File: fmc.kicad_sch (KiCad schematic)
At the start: 2 parts, among them P1 ASP-134604-01, P2 ASP-134604-01

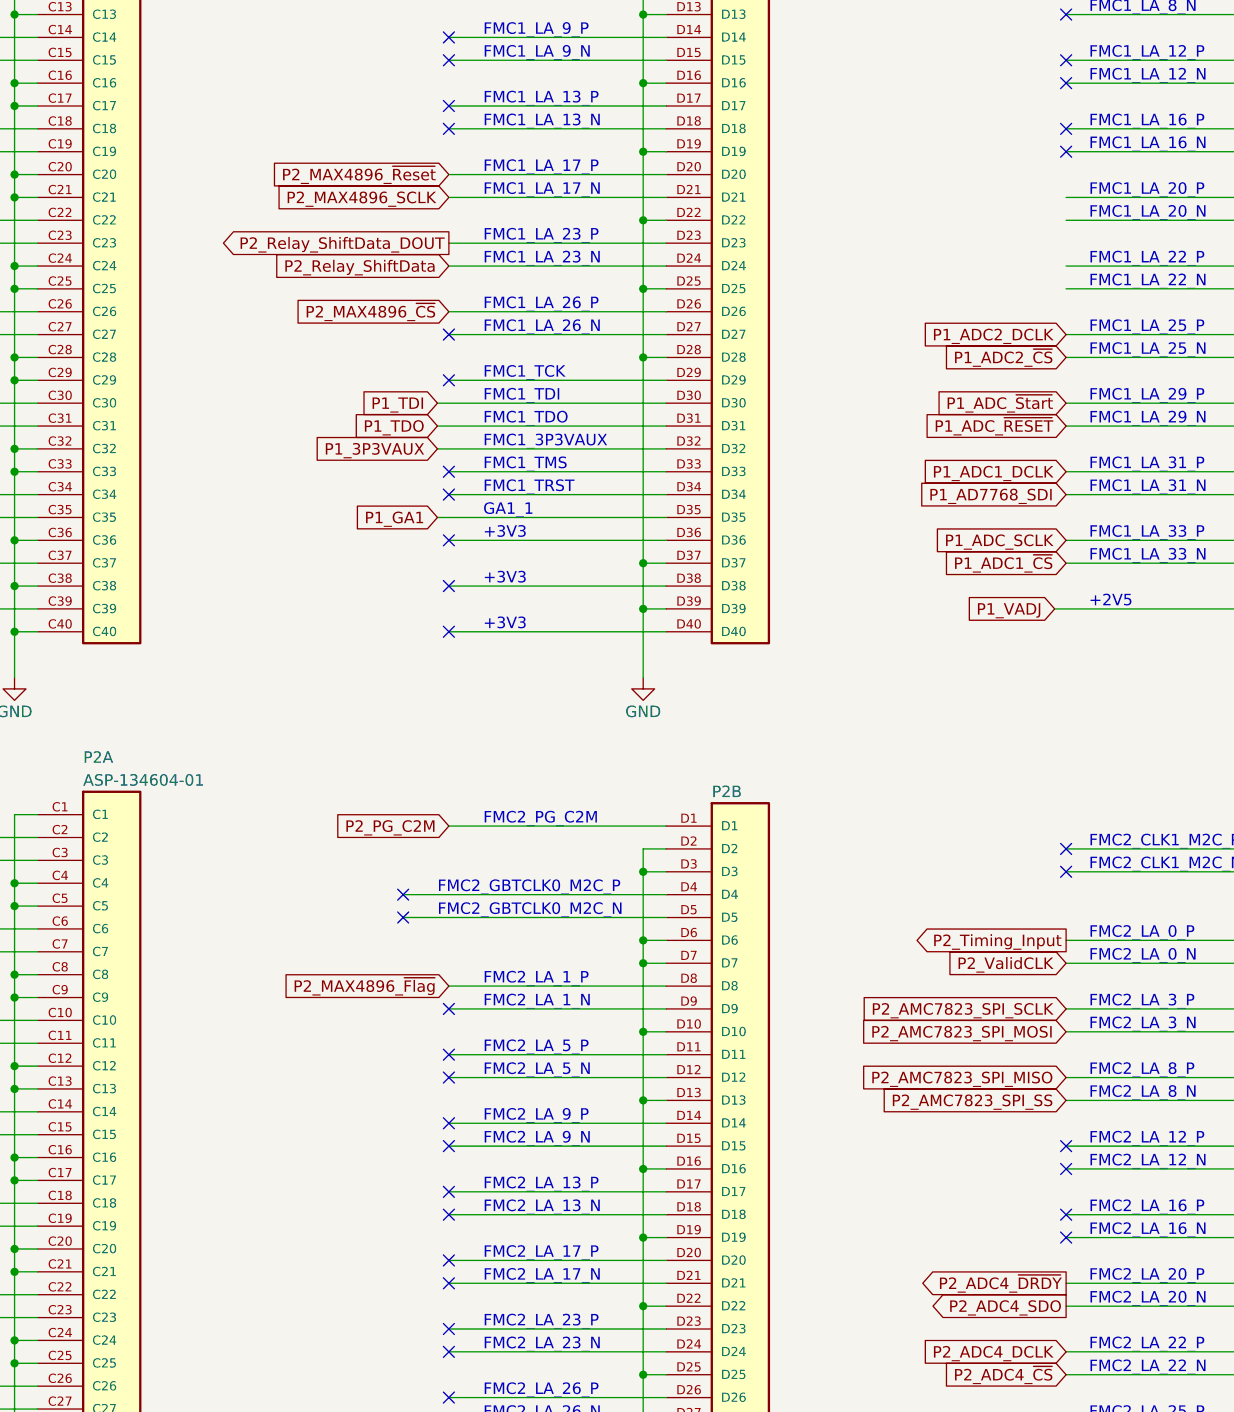
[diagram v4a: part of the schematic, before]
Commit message: Updated Project with Latest Changes
Project:
-Added pdf plots of PCB layout

Schematics:
-Fixed L8 Pinout
-Adjusted FMC connections
-Adjusted level shifter connections

Layout:
-Completed AFE/ADC/Power/Relay driver sections

Layout WIP To Complete:
-Misc. error cleanup
- Silkscreen adjust
- Add Silkscreen SN & logo
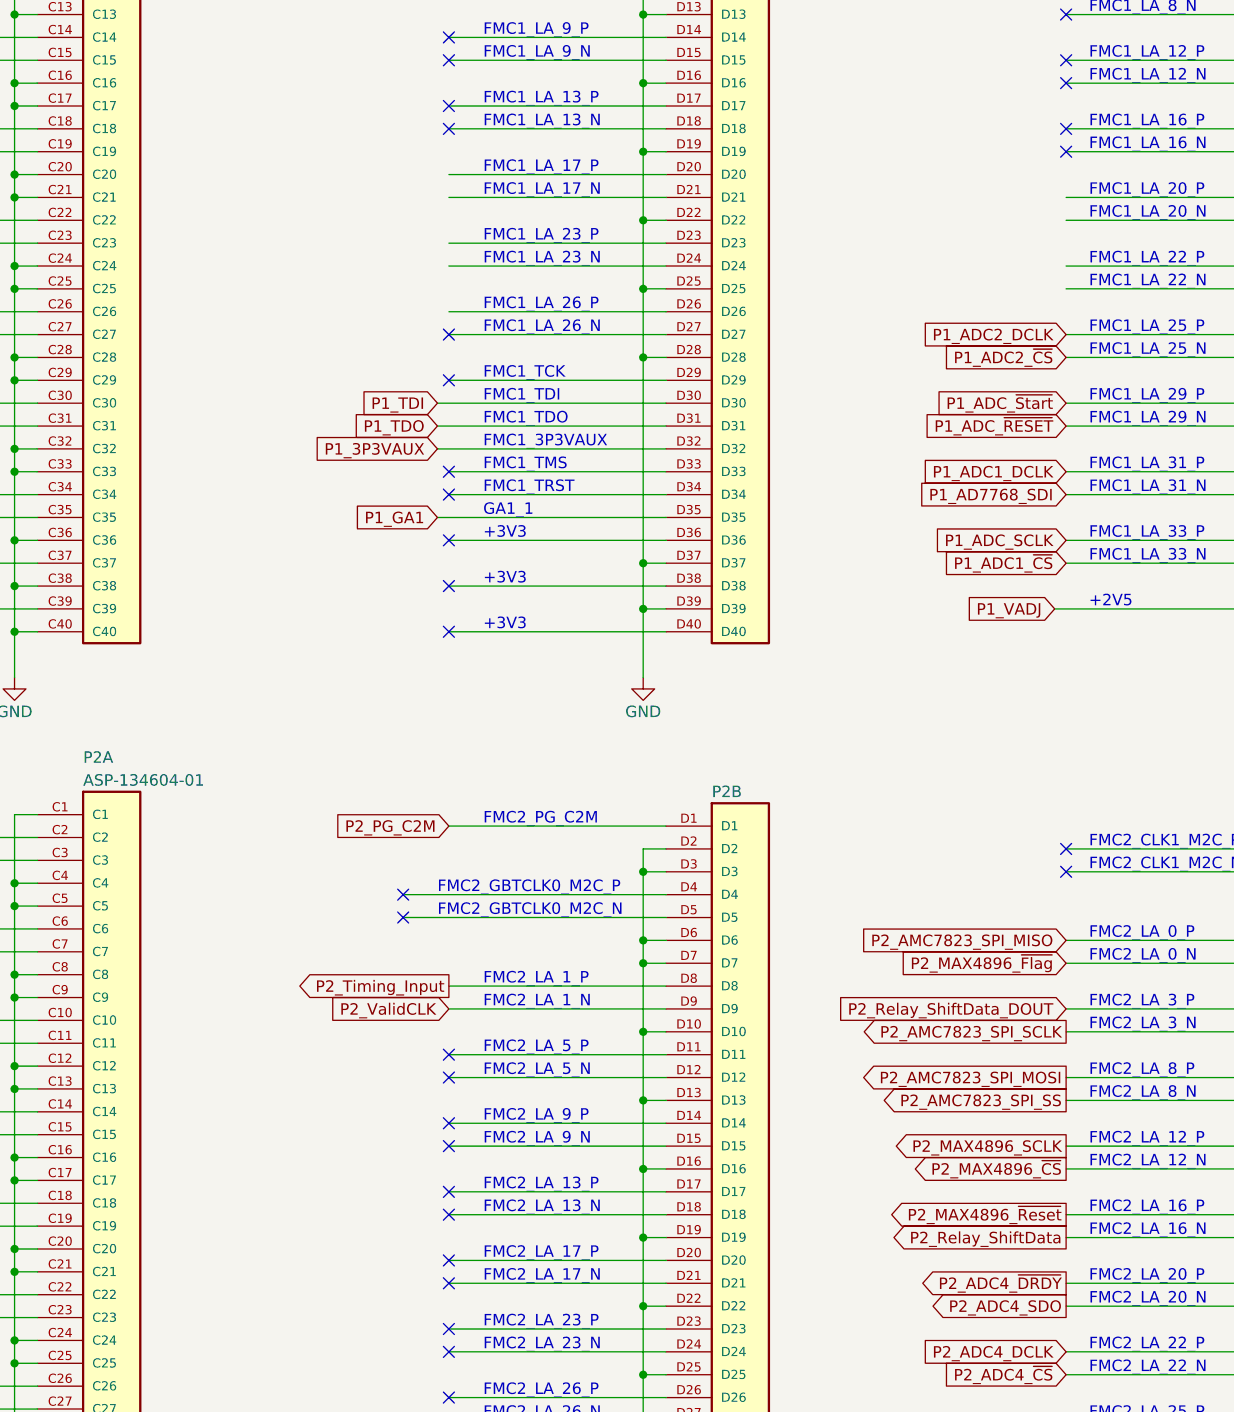
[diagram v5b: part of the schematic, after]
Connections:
- net P2_AMC7823_SPI_MISO: now also P2.G6; no longer P2.G12
- net P2_AMC7823_SPI_MOSI: now also P2.G12; no longer P2.G10
- net P2_AMC7823_SPI_SCLK: now also P2.G10; no longer P2.G9
- net P2_MAX4896_SCLK: now also P2.G15; no longer P1.D21
- net P2_MAX4896_~{CS}: now also P2.G16; no longer P1.D26
- net P2_MAX4896_~{Flag}: now also P2.G7; no longer P2.D8
- net P2_MAX4896_~{Reset}: now also P2.G18; no longer P1.D20
- net P2_Relay_ShiftData: now also P2.G19; no longer P1.D24
- net P2_Relay_ShiftData_DOUT: now also P2.G9; no longer P1.D23
- net P2_Timing_Input: now also P2.D8; no longer P2.G6
- net P2_ValidCLK: now also P2.D9; no longer P2.G7
- no-connect marks 100 -> 95
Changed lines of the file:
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@@
   )
   (no_connect (at 157.48 49.53))
-  (no_connect (at 226.06 187.96))
   (no_connect (at 157.48 102.87))
   (no_connect (at 87.63 57.15))
@@
   (no_connect (at 226.06 147.32))
   (no_connect (at 87.63 34.29))
-  (no_connect (at 226.06 177.8))
   (no_connect (at 293.37 29.21))
   (no_connect (at 87.63 54.61))
@@
   (no_connect (at 157.48 115.57))
   (no_connect (at 157.48 64.77))
-  (no_connect (at 157.48 162.56))
   (no_connect (at 293.37 153.67))
   (no_connect (at 157.48 110.49))
@@
   (no_connect (at 157.48 167.64))
   (no_connect (at 157.48 57.15))
-  (no_connect (at 226.06 185.42))
   (no_connect (at 87.63 186.69))
-  (no_connect (at 226.06 180.34))
   (no_connect (at 157.48 175.26))
   (no_connect (at 157.48 21.59))
@@
     (effects (font (size 1.27 1.27)) (justify left bottom))
   )
-  (global_label "P2_AMC7823_SPI_MOSI" (shape input) (at 226.06 165.1 180) (fields_autoplaced)
-    (effects (font (size 1.27 1.27)) (justify right))
-    (property "Intersheetrefs" "${INTERSHEET_REFS}" (at 201.364 165.1 0)
-      (effects (font (size 1.27 1.27)) (justify right) hide)
-    )
-  )
   (global_label "P1_GA1" (shape input) (at 156.21 107.95 180) (fields_autoplaced)
     (effects (font (size 1.27 1.27)) (justify right))
@@
     )
   )
+  (global_label "P2_Timing_Input" (shape output) (at 157.48 160.02 180) (fields_autoplaced)
+    (effects (font (size 1.27 1.27)) (justify right))
+    (property "Intersheetrefs" "${INTERSHEET_REFS}" (at 139.1341 160.02 0)
+      (effects (font (size 1.27 1.27)) (justify right) hide)
+    )
+  )
   (global_label "ADC3_DO2" (shape input) (at 293.37 214.63 180) (fields_autoplaced)
     (effects (font (size 1.27 1.27)) (justify right))
@@
     )
   )
-  (global_label "P2_ValidCLK" (shape input) (at 226.06 157.48 180) (fields_autoplaced)
-    (effects (font (size 1.27 1.27)) (justify right))
-    (property "Intersheetrefs" "${INTERSHEET_REFS}" (at 211.4824 157.48 0)
+  (global_label "P2_Relay_ShiftData" (shape output) (at 226.06 187.96 180) (fields_autoplaced)
+    (effects (font (size 1.27 1.27)) (justify right))
+    (property "Intersheetrefs" "${INTERSHEET_REFS}" (at 204.8907 187.96 0)
       (effects (font (size 1.27 1.27)) (justify right) hide)
     )
@@
     )
   )
-  (global_label "P2_AMC7823_SPI_SS" (shape input) (at 226.06 172.72 180) (fields_autoplaced)
-    (effects (font (size 1.27 1.27)) (justify right))
-    (property "Intersheetrefs" "${INTERSHEET_REFS}" (at 203.5412 172.72 0)
-      (effects (font (size 1.27 1.27)) (justify right) hide)
-    )
-  )
   (global_label "P1_ADC2_SDO" (shape output) (at 226.06 36.83 180) (fields_autoplaced)
     (effects (font (size 1.27 1.27)) (justify right))
@@
     )
   )
-  (global_label "P2_AMC7823_SPI_MISO" (shape input) (at 226.06 170.18 180) (fields_autoplaced)
-    (effects (font (size 1.27 1.27)) (justify right))
-    (property "Intersheetrefs" "${INTERSHEET_REFS}" (at 201.364 170.18 0)
-      (effects (font (size 1.27 1.27)) (justify right) hide)
-    )
-  )
   (global_label "P2_ADC3_~{DRDY}" (shape output) (at 293.37 196.85 180) (fields_autoplaced)
     (effects (font (size 1.27 1.27)) (justify right))
@@
     )
   )
-  (global_label "P2_Timing_Input" (shape output) (at 226.06 154.94 180) (fields_autoplaced)
-    (effects (font (size 1.27 1.27)) (justify right))
-    (property "Intersheetrefs" "${INTERSHEET_REFS}" (at 207.7141 154.94 0)
+  (global_label "P2_MAX4896_~{Reset}" (shape output) (at 226.06 185.42 180) (fields_autoplaced)
+    (effects (font (size 1.27 1.27)) (justify right))
+    (property "Intersheetrefs" "${INTERSHEET_REFS}" (at 204.951 185.42 0)
       (effects (font (size 1.27 1.27)) (justify right) hide)
     )
@@
     )
   )
-  (global_label "P2_MAX4896_~{Flag}" (shape input) (at 157.48 160.02 180) (fields_autoplaced)
-    (effects (font (size 1.27 1.27)) (justify right))
-    (property "Intersheetrefs" "${INTERSHEET_REFS}" (at 137.5202 160.02 0)
-      (effects (font (size 1.27 1.27)) (justify right) hide)
-    )
-  )
   (global_label "P2_AD7768_MCLK+" (shape input) (at 293.37 158.75 180) (fields_autoplaced)
     (effects (font (size 1.27 1.27)) (justify right))
@@
     )
   )
+  (global_label "P2_MAX4896_~{Flag}" (shape input) (at 226.06 157.48 180) (fields_autoplaced)
+    (effects (font (size 1.27 1.27)) (justify right))
+    (property "Intersheetrefs" "${INTERSHEET_REFS}" (at 206.1002 157.48 0)
+      (effects (font (size 1.27 1.27)) (justify right) hide)
+    )
+  )
   (global_label "ADC4_DO5" (shape input) (at 293.37 181.61 180) (fields_autoplaced)
     (effects (font (size 1.27 1.27)) (justify right))
@@
     )
   )
+  (global_label "P2_AMC7823_SPI_SS" (shape output) (at 226.06 172.72 180) (fields_autoplaced)
+    (effects (font (size 1.27 1.27)) (justify right))
+    (property "Intersheetrefs" "${INTERSHEET_REFS}" (at 203.6206 172.72 0)
+      (effects (font (size 1.27 1.27)) (justify right) hide)
+    )
+  )
   (global_label "ADC2_DO3" (shape input) (at 293.37 52.07 180) (fields_autoplaced)
     (effects (font (size 1.27 1.27)) (justify right))
@@
     )
   )
-  (global_label "P2_MAX4896_SCLK" (shape input) (at 157.48 72.39 180) (fields_autoplaced)
-    (effects (font (size 1.27 1.27)) (justify right))
-    (property "Intersheetrefs" "${INTERSHEET_REFS}" (at 136.715 72.39 0)
-      (effects (font (size 1.27 1.27)) (justify right) hide)
-    )
-  )
-  (global_label "P2_MAX4896_~{Reset}" (shape input) (at 157.48 69.85 180) (fields_autoplaced)
-    (effects (font (size 1.27 1.27)) (justify right))
-    (property "Intersheetrefs" "${INTERSHEET_REFS}" (at 136.2916 69.85 0)
-      (effects (font (size 1.27 1.27)) (justify right) hide)
-    )
-  )
   (global_label "P1_ADC_~{Start}" (shape input) (at 226.06 95.25 180) (fields_autoplaced)
     (effects (font (size 1.27 1.27)) (justify right))
@@
     )
   )
-  (global_label "P2_MAX4896_~{CS}" (shape input) (at 157.48 85.09 180) (fields_autoplaced)
-    (effects (font (size 1.27 1.27)) (justify right))
-    (property "Intersheetrefs" "${INTERSHEET_REFS}" (at 139.0131 85.09 0)
-      (effects (font (size 1.27 1.27)) (justify right) hide)
-    )
-  )
   (global_label "P1_ADC1_~{CS}" (shape input) (at 226.06 113.03 180) (fields_autoplaced)
     (effects (font (size 1.27 1.27)) (justify right))
@@
     )
   )
+  (global_label "P2_AMC7823_SPI_SCLK" (shape output) (at 226.06 165.1 180) (fields_autoplaced)
+    (effects (font (size 1.27 1.27)) (justify right))
+    (property "Intersheetrefs" "${INTERSHEET_REFS}" (at 201.262 165.1 0)
+      (effects (font (size 1.27 1.27)) (justify right) hide)
+    )
+  )
   (global_label "ADC3_DO3" (shape input) (at 293.37 219.71 180) (fields_autoplaced)
     (effects (font (size 1.27 1.27)) (justify right))
@@
     )
   )
-  (global_label "P2_Relay_ShiftData_DOUT" (shape output) (at 157.48 77.47 180) (fields_autoplaced)
-    (effects (font (size 1.27 1.27)) (justify right))
-    (property "Intersheetrefs" "${INTERSHEET_REFS}" (at 130.3651 77.47 0)
-      (effects (font (size 1.27 1.27)) (justify right) hide)
-    )
-  )
-  (global_label "P2_Relay_ShiftData" (shape input) (at 157.48 80.01 180) (fields_autoplaced)
-    (effects (font (size 1.27 1.27)) (justify right))
-    (property "Intersheetrefs" "${INTERSHEET_REFS}" (at 136.2313 80.01 0)
-      (effects (font (size 1.27 1.27)) (justify right) hide)
-    )
-  )
-  (global_label "P2_AMC7823_SPI_SCLK" (shape input) (at 226.06 162.56 180) (fields_autoplaced)
-    (effects (font (size 1.27 1.27)) (justify right))
-    (property "Intersheetrefs" "${INTERSHEET_REFS}" (at 201.1826 162.56 0)
+  (global_label "P2_ValidCLK" (shape input) (at 157.48 162.56 180) (fields_autoplaced)
+    (effects (font (size 1.27 1.27)) (justify right))
+    (property "Intersheetrefs" "${INTERSHEET_REFS}" (at 142.9024 162.56 0)
       (effects (font (size 1.27 1.27)) (justify right) hide)
     )
@@
     )
   )
+  (global_label "P2_MAX4896_~{CS}" (shape output) (at 226.06 180.34 180) (fields_autoplaced)
+    (effects (font (size 1.27 1.27)) (justify right))
+    (property "Intersheetrefs" "${INTERSHEET_REFS}" (at 207.6725 180.34 0)
+      (effects (font (size 1.27 1.27)) (justify right) hide)
+    )
+  )
   (global_label "ADC1_DO1" (shape input) (at 293.37 90.17 180) (fields_autoplaced)
     (effects (font (size 1.27 1.27)) (justify right))
@@
     )
   )
+  (global_label "P2_Relay_ShiftData_DOUT" (shape input) (at 226.06 162.56 180) (fields_autoplaced)
+    (effects (font (size 1.27 1.27)) (justify right))
+    (property "Intersheetrefs" "${INTERSHEET_REFS}" (at 199.0245 162.56 0)
+      (effects (font (size 1.27 1.27)) (justify right) hide)
+    )
+  )
+  (global_label "P2_MAX4896_SCLK" (shape output) (at 226.06 177.8 180) (fields_autoplaced)
+    (effects (font (size 1.27 1.27)) (justify right))
+    (property "Intersheetrefs" "${INTERSHEET_REFS}" (at 205.3744 177.8 0)
+      (effects (font (size 1.27 1.27)) (justify right) hide)
+    )
+  )
+  (global_label "P2_AMC7823_SPI_MISO" (shape input) (at 226.06 154.94 180) (fields_autoplaced)
+    (effects (font (size 1.27 1.27)) (justify right))
+    (property "Intersheetrefs" "${INTERSHEET_REFS}" (at 201.4434 154.94 0)
+      (effects (font (size 1.27 1.27)) (justify right) hide)
+    )
+  )
   (global_label "ADC1_DO6" (shape input) (at 293.37 107.95 180) (fields_autoplaced)
     (effects (font (size 1.27 1.27)) (justify right))
@@
       (effects (font (size 1.27 1.27)) (justify right) hide)
     )
+  )
+  (global_label "P2_AMC7823_SPI_MOSI" (shape output) (at 226.06 170.18 180) (fields_autoplaced)
+    (effects (font (size 1.27 1.27)) (justify right))
+    (property "Intersheetrefs" "${INTERSHEET_REFS}" (at 201.4434 170.18 0)
+      (effects (font (size 1.27 1.27)) (justify right) hide)
+    )
